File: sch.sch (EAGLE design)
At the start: 1 part, among them U1 Value

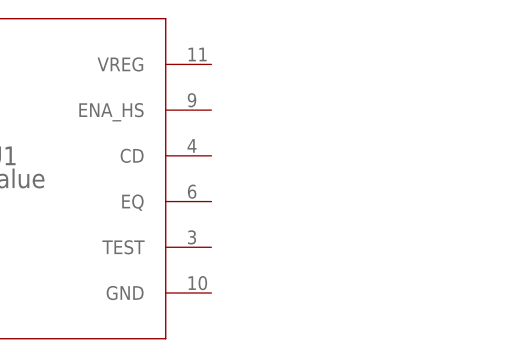
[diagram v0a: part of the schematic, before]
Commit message: Added female usb
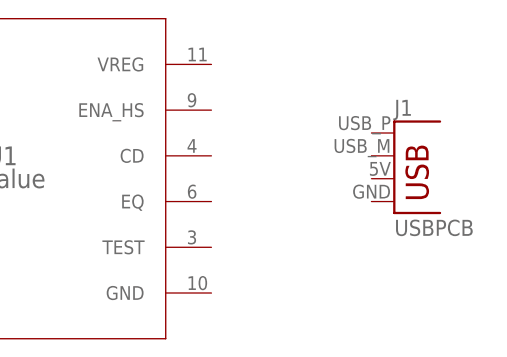
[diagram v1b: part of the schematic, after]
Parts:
- added J1: USBPCB, SparkFun-Connectors:USBPCB
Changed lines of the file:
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@@
 <layer number="48" name="Document" color="7" fill="1" visible="no" active="no"/>
 <layer number="49" name="Reference" color="7" fill="1" visible="no" active="no"/>
+<layer number="50" name="dxf" color="7" fill="1" visible="no" active="no"/>
 <layer number="51" name="tDocu" color="7" fill="1" visible="no" active="no"/>
 <layer number="52" name="bDocu" color="7" fill="1" visible="no" active="no"/>
+<layer number="53" name="tGND_GNDA" color="7" fill="9" visible="no" active="no"/>
+<layer number="54" name="bGND_GNDA" color="1" fill="9" visible="no" active="no"/>
+<layer number="56" name="wert" color="7" fill="1" visible="no" active="no"/>
+<layer number="57" name="tCAD" color="7" fill="1" visible="no" active="no"/>
+<layer number="59" name="tCarbon" color="7" fill="1" visible="no" active="no"/>
+<layer number="60" name="bCarbon" color="7" fill="1" visible="no" active="no"/>
 <layer number="90" name="Modules" color="5" fill="1" visible="yes" active="yes"/>
 <layer number="91" name="Nets" color="2" fill="1" visible="yes" active="yes"/>
@@
 <layer number="97" name="Info" color="7" fill="1" visible="yes" active="yes"/>
 <layer number="98" name="Guide" color="6" fill="1" visible="yes" active="yes"/>
+<layer number="99" name="SpiceOrder" color="7" fill="1" visible="yes" active="yes"/>
+<layer number="100" name="Muster" color="7" fill="1" visible="no" active="no"/>
+<layer number="101" name="Patch_Top" color="12" fill="4" visible="yes" active="yes"/>
+<layer number="102" name="Vscore" color="7" fill="1" visible="yes" active="yes"/>
+<layer number="103" name="tMap" color="7" fill="1" visible="yes" active="yes"/>
+<layer number="104" name="Name" color="16" fill="1" visible="yes" active="yes"/>
+<layer number="105" name="tPlate" color="7" fill="1" visible="yes" active="yes"/>
+<layer number="106" name="bPlate" color="7" fill="1" visible="yes" active="yes"/>
+<layer number="107" name="Crop" color="7" fill="1" visible="yes" active="yes"/>
+<layer number="108" name="tplace-old" color="10" fill="1" visible="yes" active="yes"/>
+<layer number="109" name="ref-old" color="11" fill="1" visible="yes" active="yes"/>
+<layer number="110" name="fp0" color="7" fill="1" visible="yes" active="yes"/>
+<layer number="111" name="LPC17xx" color="7" fill="1" visible="yes" active="yes"/>
+<layer number="112" name="tSilk" color="7" fill="1" visible="yes" active="yes"/>
+<layer number="113" name="IDFDebug" color="4" fill="1" visible="yes" active="yes"/>
+<layer number="114" name="Badge_Outline" color="7" fill="1" visible="yes" active="yes"/>
+<layer number="115" name="ReferenceISLANDS" color="7" fill="1" visible="yes" active="yes"/>
+<layer number="116" name="Patch_BOT" color="9" fill="4" visible="yes" active="yes"/>
+<layer number="118" name="Rect_Pads" color="7" fill="1" visible="yes" active="yes"/>
+<layer number="121" name="_tsilk" color="7" fill="1" visible="yes" active="yes"/>
+<layer number="122" name="_bsilk" color="7" fill="1" visible="yes" active="yes"/>
+<layer number="123" name="tTestmark" color="7" fill="1" visible="yes" active="yes"/>
+<layer number="124" name="bTestmark" color="7" fill="1" visible="yes" active="yes"/>
+<layer number="125" name="_tNames" color="7" fill="1" visible="yes" active="yes"/>
+<layer number="126" name="_bNames" color="7" fill="1" visible="yes" active="yes"/>
+<layer number="127" name="_tValues" color="7" fill="1" visible="yes" active="yes"/>
+<layer number="128" name="_bValues" color="7" fill="1" visible="yes" active="yes"/>
+<layer number="129" name="Mask" color="7" fill="1" visible="yes" active="yes"/>
+<layer number="131" name="tAdjust" color="7" fill="1" visible="yes" active="yes"/>
+<layer number="132" name="bAdjust" color="7" fill="1" visible="yes" active="yes"/>
+<layer number="144" name="Drill_legend" color="7" fill="1" visible="yes" active="yes"/>
+<layer number="150" name="Notes" color="7" fill="1" visible="yes" active="yes"/>
+<layer number="151" name="HeatSink" color="7" fill="1" visible="yes" active="yes"/>
+<layer number="152" name="_bDocu" color="7" fill="1" visible="yes" active="yes"/>
+<layer number="153" name="FabDoc1" color="7" fill="1" visible="yes" active="yes"/>
+<layer number="154" name="FabDoc2" color="7" fill="1" visible="yes" active="yes"/>
+<layer number="155" name="FabDoc3" color="7" fill="1" visible="yes" active="yes"/>
+<layer number="199" name="Contour" color="7" fill="1" visible="yes" active="yes"/>
+<layer number="200" name="200bmp" color="1" fill="10" visible="yes" active="yes"/>
+<layer number="201" name="201bmp" color="2" fill="10" visible="yes" active="yes"/>
+<layer number="202" name="202bmp" color="3" fill="10" visible="yes" active="yes"/>
+<layer number="203" name="203bmp" color="4" fill="10" visible="yes" active="yes"/>
+<layer number="204" name="204bmp" color="5" fill="10" visible="yes" active="yes"/>
+<layer number="205" name="205bmp" color="6" fill="10" visible="yes" active="yes"/>
+<layer number="206" name="206bmp" color="7" fill="10" visible="yes" active="yes"/>
+<layer number="207" name="207bmp" color="8" fill="10" visible="yes" active="yes"/>
+<layer number="208" name="208bmp" color="9" fill="10" visible="yes" active="yes"/>
+<layer number="209" name="209bmp" color="7" fill="1" visible="yes" active="yes"/>
+<layer number="210" name="210bmp" color="7" fill="1" visible="yes" active="yes"/>
+<layer number="211" name="211bmp" color="7" fill="1" visible="yes" active="yes"/>
+<layer number="212" name="212bmp" color="7" fill="1" visible="yes" active="yes"/>
+<layer number="213" name="213bmp" color="7" fill="1" visible="yes" active="yes"/>
+<layer number="214" name="214bmp" color="7" fill="1" visible="yes" active="yes"/>
+<layer number="215" name="215bmp" color="7" fill="1" visible="yes" active="yes"/>
+<layer number="216" name="216bmp" color="7" fill="1" visible="yes" active="yes"/>
+<layer number="217" name="217bmp" color="18" fill="1" visible="no" active="no"/>
+<layer number="218" name="218bmp" color="19" fill="1" visible="no" active="no"/>
+<layer number="219" name="219bmp" color="20" fill="1" visible="no" active="no"/>
+<layer number="220" name="220bmp" color="21" fill="1" visible="no" active="no"/>
+<layer number="221" name="221bmp" color="22" fill="1" visible="no" active="no"/>
+<layer number="222" name="222bmp" color="23" fill="1" visible="no" active="no"/>
+<layer number="223" name="223bmp" color="24" fill="1" visible="no" active="no"/>
+<layer number="224" name="224bmp" color="25" fill="1" visible="no" active="no"/>
+<layer number="225" name="225bmp" color="7" fill="1" visible="yes" active="yes"/>
+<layer number="226" name="226bmp" color="7" fill="1" visible="yes" active="yes"/>
+<layer number="227" name="227bmp" color="7" fill="1" visible="yes" active="yes"/>
+<layer number="228" name="228bmp" color="7" fill="1" visible="yes" active="yes"/>
+<layer number="229" name="229bmp" color="7" fill="1" visible="yes" active="yes"/>
+<layer number="230" name="230bmp" color="7" fill="1" visible="yes" active="yes"/>
+<layer number="231" name="231bmp" color="7" fill="1" visible="yes" active="yes"/>
+<layer number="248" name="Housing" color="7" fill="1" visible="yes" active="yes"/>
+<layer number="249" name="Edge" color="7" fill="1" visible="yes" active="yes"/>
+<layer number="250" name="Descript" color="3" fill="1" visible="no" active="no"/>
+<layer number="251" name="SMDround" color="12" fill="11" visible="no" active="no"/>
+<layer number="254" name="cooling" color="7" fill="1" visible="yes" active="yes"/>
+<layer number="255" name="routoute" color="7" fill="1" visible="yes" active="yes"/>
 </layers>
 <schematic xreflabel="%F%N/%S.%C%R" xrefpart="/%S.%C%R">
@@
 <parts>
 <part name="U1" library="TUSB211" deviceset="TUSB211RWBR" device="" value="Value"/>
+<part name="J1" library="SparkFun-Connectors" deviceset="USB" device="PCB"/>
 </parts>
 <sheets>
@@
 <instances>
 <instance part="U1" gate="A" x="66.04" y="60.96"/>
+<instance part="J1" gate="G$1" x="106.68" y="58.42"/>
 </instances>
 <busses>

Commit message: version 1
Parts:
- removed J1: USBPCB, SparkFun-Connectors:USBPCB
- added BOARDTOPI: USBPCB, USBPCB:USBPCB
- added C1, C4: 0.1uF, SparkFun-Capacitors:0.1UF-0603-25V-(+80/-20%)
- added C2, C6: 1.0uF, SparkFun-Capacitors:1.0UF-0603-16V-10%
- added C3: 10nF, SparkFun-Capacitors:10NF-0603-50V-10%
- added D1: Red, SparkFun-LED:LED-RED0603-SMART
- added R1: 120, rcl:R-US_R0805
- added USBSMD: USB, USBSMD:USB
- added VOLTAGEREGULATOR: INA169, SparkFun-IC-Special-Function:INA169
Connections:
- new net 3.3V: C2.1, C3.2, U1.VCC, VOLTAGEREGULATOR.V+
- new net EQ: U1.EQ
- new net GND: BOARDTOPI.GND, C1.1, C2.2, C3.1, C4.2, C6.1, D1.C, U1.GND, USBSMD.GND, VOLTAGEREGULATOR.GND
- new net M: BOARDTOPI.D-, U1.D1M, U1.D2M, USBSMD.D-
- new net N$1: C1.2, U1.VREG
- new net N$2: D1.A, R1.1
- new net N$3: R1.2, U1.CD
- new net N$4: C4.1, U1.RSTN
- new net NC/ADJ: VOLTAGEREGULATOR.VIN-
- new net P: BOARDTOPI.D+, U1.D1P, U1.D2P, USBSMD.D+
- new net VIN: BOARDTOPI.VCC, C6.2, USBSMD.VCC, VOLTAGEREGULATOR.OUT, VOLTAGEREGULATOR.VIN+
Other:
- note added: "Shutdown"
- note added: "Vout"
- moved on the sheet: U1
